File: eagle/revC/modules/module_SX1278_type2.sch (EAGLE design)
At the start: 19 parts, among them X1 734120110

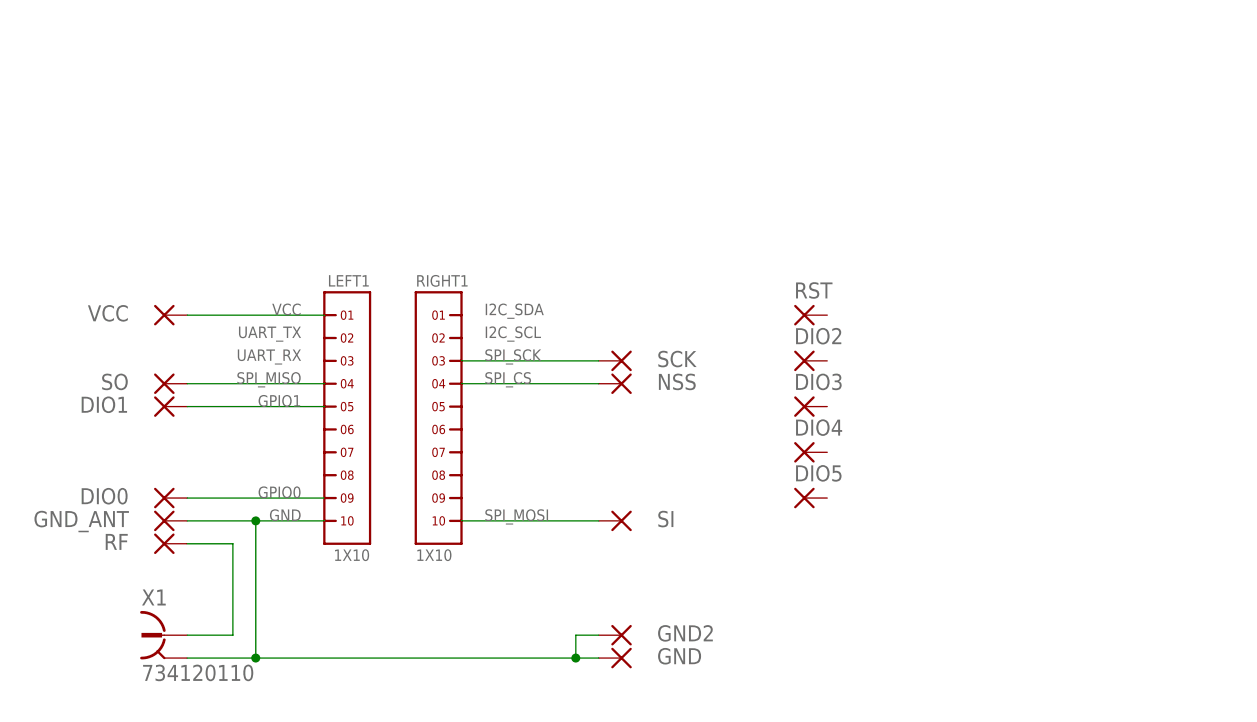
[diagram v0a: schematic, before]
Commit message: Replaced modules with library parts
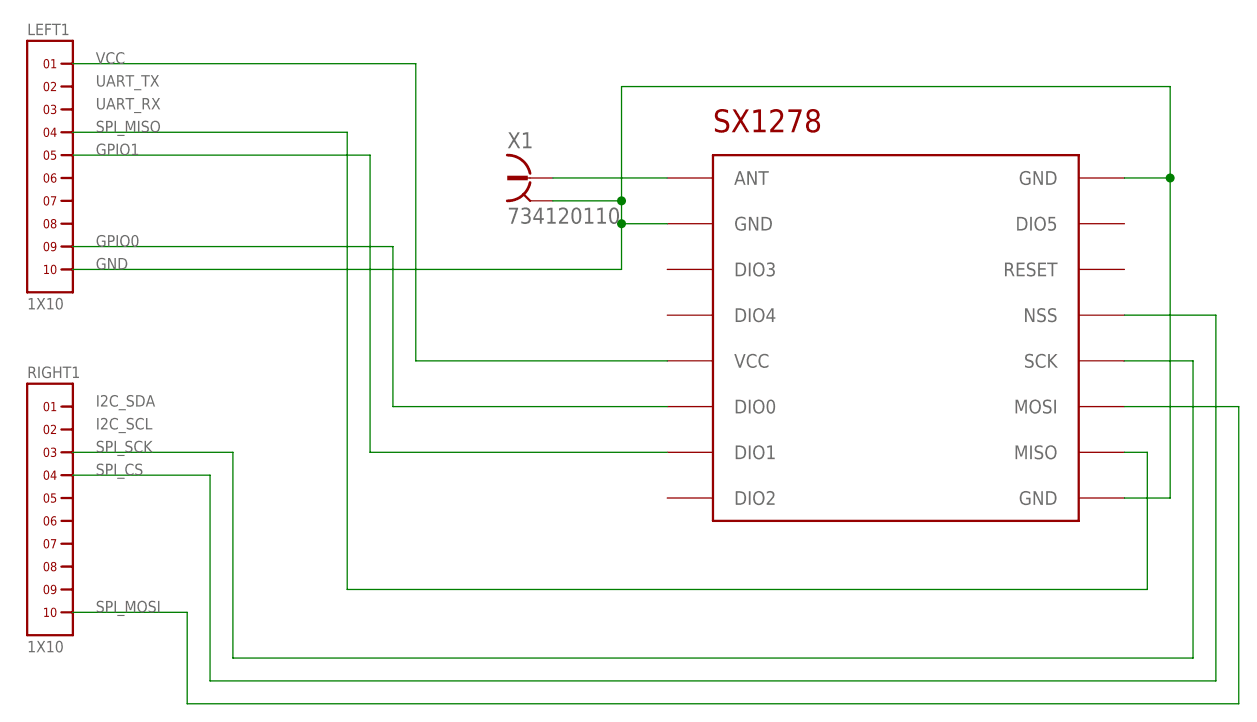
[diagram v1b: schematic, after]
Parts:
- removed DIO0, DIO1, DIO2, DIO3, DIO4, DIO5, GND, GND2, GND_ANT, NSS, RF, RST, SCK, SI, SO, VCC: (no value), wirepad:SMD2
- added U$1: SX1278_2, RadioShield:SX1278_2
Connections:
- removed net ANT: RF.P, X1.1
- removed net INT0: DIO0.P, LEFT1.9
- removed net INT1: DIO1.P, LEFT1.5
- removed net SCPI_SCK: RIGHT1.3, SCK.P
- removed net SPI_CS: NSS.P, RIGHT1.4
- removed net SPI_MISO: LEFT1.4, SO.P
- removed net SPI_MOSI: RIGHT1.10, SI.P
- removed net VCC: LEFT1.1, VCC.P
- new net N$1: U$1.ANT, X1.1
- new net N$2: LEFT1.9, U$1.DIO0
- new net N$3: RIGHT1.10, U$1.MOSI
- new net N$4: RIGHT1.4, U$1.NSS
- new net N$5: RIGHT1.3, U$1.SCK
- new net N$6: LEFT1.5, U$1.DIO1
- new net N$7: LEFT1.4, U$1.MISO
- new net N$8: LEFT1.1, U$1.VCC
- net GND: now also U$1.GND@1, U$1.GND@2, U$1.GND@3; no longer GND.P, GND2.P, GND_ANT.P
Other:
- moved on the sheet: LEFT1, RIGHT1, X1
